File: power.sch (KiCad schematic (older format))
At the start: 43 parts, among them J5 Conn_01x02, Q1 Q_NMOS_GSD, Q2 AON7405, Q3 Q_NMOS_GSD, U7 MP8759GD, U8 NCP133AMX150TCG

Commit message: re-layout power input switcher
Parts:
- R21: footprint Resistor_SMD:R_0402_1005Metric -> Resistor_SMD:R_0603_1608Metric
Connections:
- net FB: now reaches R26.1, R27.2, R29.2, U7.11 (FB)
- net EN: now reaches C93.1, R18.2, R19.1, U7.12 (EN)
- net MODE: now reaches R20.1, R22.1, U7.6 (MODE)
- net SW: now reaches C94.2, L7.1, R25.2, U7.7 (SW)
- net BST: now reaches R21.2, U7.8 (BST)
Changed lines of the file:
@@
 F 0 "R21" V 6993 1750 50  0000 C CNN
 F 1 "3.3" V 7084 1750 50  0000 C CNN
-F 2 "Resistor_SMD:R_0402_1005Metric" V 7130 1750 50  0001 C CNN
+F 2 "Resistor_SMD:R_0603_1608Metric" V 7130 1750 50  0001 C CNN
 F 3 "~" H 7200 1750 50  0001 C CNN
 	1    7200 1750
@@
 Wire Wire Line
 	2600 3600 2700 3600
+Text Label 7350 2500 0    50   ~ 0
+SW
+Text Label 7350 3150 0    50   ~ 0
+FB
+Text Label 5750 2850 0    50   ~ 0
+EN
+Text Label 6100 3250 0    50   ~ 0
+MODE
+Text Label 6800 2100 0    50   ~ 0
+BST
 $EndSCHEMATC

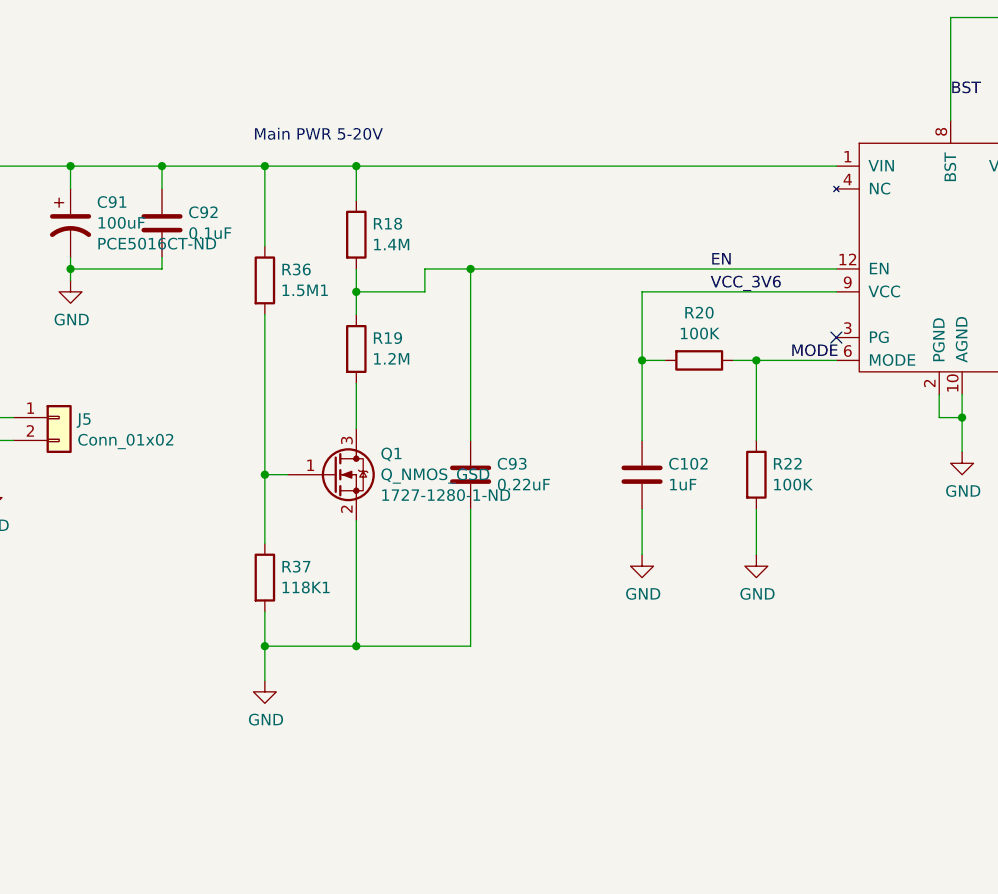
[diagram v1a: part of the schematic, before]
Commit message: Add zener instead of fet to limit voltage on power input EN
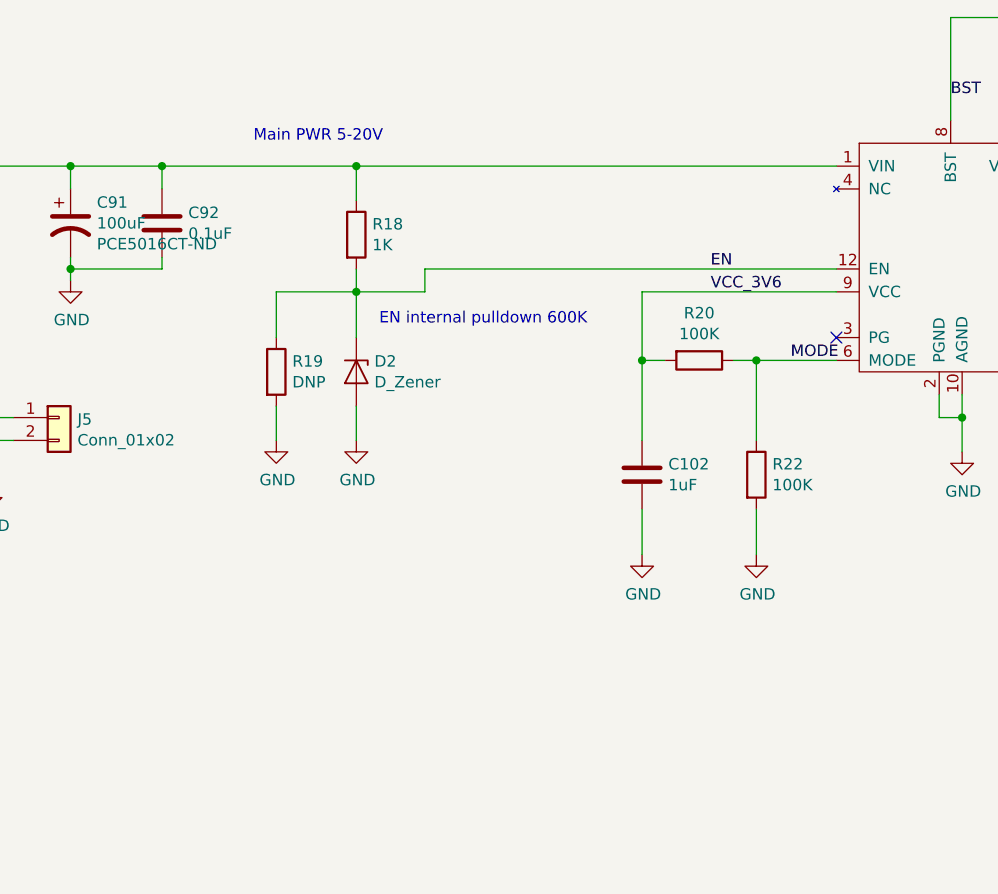
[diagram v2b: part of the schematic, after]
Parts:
- removed C93: 0.22uF, Capacitor_SMD:C_0402_1005Metric, symbol Device:C
- removed Q1: Q_NMOS_GSD, Package_TO_SOT_SMD:SOT-323_SC-70, symbol Device:Q_NMOS_GSD
- removed R36: 1.5M1, Resistor_SMD:R_0402_1005Metric, symbol Device:R
- removed R37: 118K1, Resistor_SMD:R_0402_1005Metric, symbol Device:R
- added D2: D_Zener, Diode_SMD:D_SOD-323, symbol Device:D_Zener
- R18: value 1.4M -> 1K
- R19: value 1.2M -> DNP
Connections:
- net EN: now also D2.1 (K)
- net GND: now also R19.2, D2.2 (A)
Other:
- note added: "EN internal pulldown 600K"
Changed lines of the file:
@@
 EESchema Schematic File Version 4
+LIBS:mxenc-cache
 EELAYER 29 0
 EELAYER END
@@
 	6300 2400 4200 2400
 $Comp
-L Device:Q_NMOS_GSD Q1
-U 1 1 5DC87C75
-P 4100 3750
-F 0 "Q1" H 4306 3841 50  0000 L CNN
-F 1 "Q_NMOS_GSD" H 4306 3750 50  0000 L CNN
-F 2 "Package_TO_SOT_SMD:SOT-323_SC-70" H 4300 3850 50  0001 C CNN
-F 3 "~" H 4100 3750 50  0001 C CNN
-F 4 "1727-1280-1-ND" H 4306 3659 50  0000 L CNN "Vendorpart"
-F 5 "NX3008NBKW,115" H 4100 3750 50  0001 C CNN "Part"
-	1    4100 3750
-	1    0    0    -1
-$EndComp
-$Comp
-L Device:R R36
-U 1 1 5DC8BFE6
-P 3800 2900
-F 0 "R36" H 3870 2946 50  0000 L CNN
-F 1 "1.5M1" H 3870 2855 50  0000 L CNN
-F 2 "Resistor_SMD:R_0402_1005Metric" V 3730 2900 50  0001 C CNN
-F 3 "~" H 3800 2900 50  0001 C CNN
-	1    3800 2900
-	1    0    0    -1
-$EndComp
-$Comp
-L Device:R R37
-U 1 1 5DC8C35A
-P 3800 4200
-F 0 "R37" H 3870 4246 50  0000 L CNN
-F 1 "118K1" H 3870 4155 50  0000 L CNN
-F 2 "Resistor_SMD:R_0402_1005Metric" V 3730 4200 50  0001 C CNN
-F 3 "~" H 3800 4200 50  0001 C CNN
-	1    3800 4200
-	1    0    0    -1
-$EndComp
-$Comp
 L Device:R R18
 U 1 1 5DC8CB6A
 P 4200 2700
 F 0 "R18" H 4270 2746 50  0000 L CNN
-F 1 "1.4M" H 4270 2655 50  0000 L CNN
+F 1 "1K" H 4270 2655 50  0000 L CNN
 F 2 "Resistor_SMD:R_0402_1005Metric" V 4130 2700 50  0001 C CNN
 F 3 "~" H 4200 2700 50  0001 C CNN
 	1    4200 2700
-	1    0    0    -1
-$EndComp
-$Comp
-L Device:R R19
-U 1 1 5DC8D48B
-P 4200 3200
-F 0 "R19" H 4270 3246 50  0000 L CNN
-F 1 "1.2M" H 4270 3155 50  0000 L CNN
-F 2 "Resistor_SMD:R_0402_1005Metric" V 4130 3200 50  0001 C CNN
-F 3 "~" H 4200 3200 50  0001 C CNN
-	1    4200 3200
 	1    0    0    -1
 $EndComp
@@
 	3350 2400 2950 2400
 Wire Wire Line
-	3800 2400 3800 2750
-Connection ~ 3800 2400
-Wire Wire Line
-	3800 2400 3350 2400
-Wire Wire Line
-	3800 3050 3800 3750
-Wire Wire Line
-	3800 3750 3900 3750
-Wire Wire Line
-	3800 3750 3800 4050
-Connection ~ 3800 3750
-Wire Wire Line
-	4200 3550 4200 3350
-Wire Wire Line
-	4200 3050 4200 2950
-Wire Wire Line
 	4200 2550 4200 2400
 Connection ~ 4200 2400
 Wire Wire Line
-	4200 2400 3800 2400
-Wire Wire Line
 	4200 2950 4500 2950
 Wire Wire Line
@@
 Wire Wire Line
 	4200 2950 4200 2850
-Wire Wire Line
-	4200 3950 4200 4500
-Wire Wire Line
-	4200 4500 3800 4500
-Wire Wire Line
-	3800 4500 3800 4350
-$Comp
-L power:GND #PWR0165
-U 1 1 5DC9B92E
-P 3800 4650
-F 0 "#PWR0165" H 3800 4400 50  0001 C CNN
-F 1 "GND" H 3805 4477 50  0000 C CNN
-F 2 "" H 3800 4650 50  0001 C CNN
-F 3 "" H 3800 4650 50  0001 C CNN
-	1    3800 4650
-	1    0    0    -1
-$EndComp
-Wire Wire Line
-	3800 4650 3800 4500
-Connection ~ 3800 4500
-$Comp
-L Device:C C93
-U 1 1 5DC9C3FB
-P 4700 3750
-F 0 "C93" H 4815 3796 50  0000 L CNN
-F 1 "0.22uF" H 4815 3705 50  0000 L CNN
-F 2 "Capacitor_SMD:C_0402_1005Metric" H 4738 3600 50  0001 C CNN
-F 3 "~" H 4700 3750 50  0001 C CNN
-	1    4700 3750
-	1    0    0    -1
-$EndComp
-Wire Wire Line
-	4700 3900 4700 4500
-Wire Wire Line
-	4700 4500 4200 4500
-Connection ~ 4200 4500
-Wire Wire Line
-	4700 3600 4700 2850
-Wire Wire Line
-	4500 2850 4700 2850
-Connection ~ 4700 2850
 Wire Wire Line
 	5950 3250 5950 3600
@@
 Wire Wire Line
 	5450 4100 5450 3900
-Wire Wire Line
-	4700 2850 6300 2850
 Wire Wire Line
 	5450 3250 5450 2950
@@
 Text Label 6800 2100 0    50   ~ 0
 BST
+Wire Wire Line
+	4500 2850 6300 2850
+Wire Wire Line
+	3350 2400 4200 2400
+$Comp
+L power:GND #PWR0165
+U 1 1 5DC6150E
+P 4200 3600
+F 0 "#PWR0165" H 4200 3350 50  0001 C CNN
+F 1 "GND" H 4205 3427 50  0000 C CNN
+F 2 "" H 4200 3600 50  0001 C CNN
+F 3 "" H 4200 3600 50  0001 C CNN
+	1    4200 3600
+	1    0    0    -1
+$EndComp
+$Comp
+L Device:D_Zener D2
+U 1 1 5DC62380
+P 4200 3300
+F 0 "D2" V 4154 3379 50  0000 L CNN
+F 1 "D_Zener" V 4245 3379 50  0000 L CNN
+F 2 "Diode_SMD:D_SOD-323" H 4200 3300 50  0001 C CNN
+F 3 "~" H 4200 3300 50  0001 C CNN
+F 4 "MM3Z4V3ST1GOSCT-ND" H 4200 3300 50  0001 C CNN "Vendorpart"
+F 5 "MM3Z4V3ST1G" H 4200 3300 50  0001 C CNN "Part"
+	1    4200 3300
+	0    1    1    0
+$EndComp
+Wire Wire Line
+	4200 2950 4200 3150
+Wire Wire Line
+	4200 3600 4200 3450
+Text Notes 4300 3100 0    50   ~ 0
+EN internal pulldown 600K
+$Comp
+L Device:R R19
+U 1 1 5D9BE1EB
+P 3850 3300
+F 0 "R19" H 3920 3346 50  0000 L CNN
+F 1 "DNP" H 3920 3255 50  0000 L CNN
+F 2 "Resistor_SMD:R_0402_1005Metric" V 3780 3300 50  0001 C CNN
+F 3 "~" H 3850 3300 50  0001 C CNN
+	1    3850 3300
+	1    0    0    -1
+$EndComp
+$Comp
+L power:GND #PWR0262
+U 1 1 5D9BE857
+P 3850 3600
+F 0 "#PWR0262" H 3850 3350 50  0001 C CNN
+F 1 "GND" H 3855 3427 50  0000 C CNN
+F 2 "" H 3850 3600 50  0001 C CNN
+F 3 "" H 3850 3600 50  0001 C CNN
+	1    3850 3600
+	1    0    0    -1
+$EndComp
+Wire Wire Line
+	3850 3600 3850 3450
+Wire Wire Line
+	3850 3150 3850 2950
+Wire Wire Line
+	3850 2950 4200 2950
 $EndSCHEMATC

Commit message: improved 5v power supply routing
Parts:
- R23: footprint Resistor_SMD:R_0402_1005Metric -> Resistor_SMD:R_0805_2012Metric
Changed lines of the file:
@@
 F 0 "R23" V 10693 2400 50  0000 C CNN
 F 1 "0" V 10784 2400 50  0000 C CNN
-F 2 "Resistor_SMD:R_0402_1005Metric" V 10830 2400 50  0001 C CNN
+F 2 "Resistor_SMD:R_0805_2012Metric" V 10830 2400 50  0001 C CNN
 F 3 "~" H 10900 2400 50  0001 C CNN
 	1    10900 2400

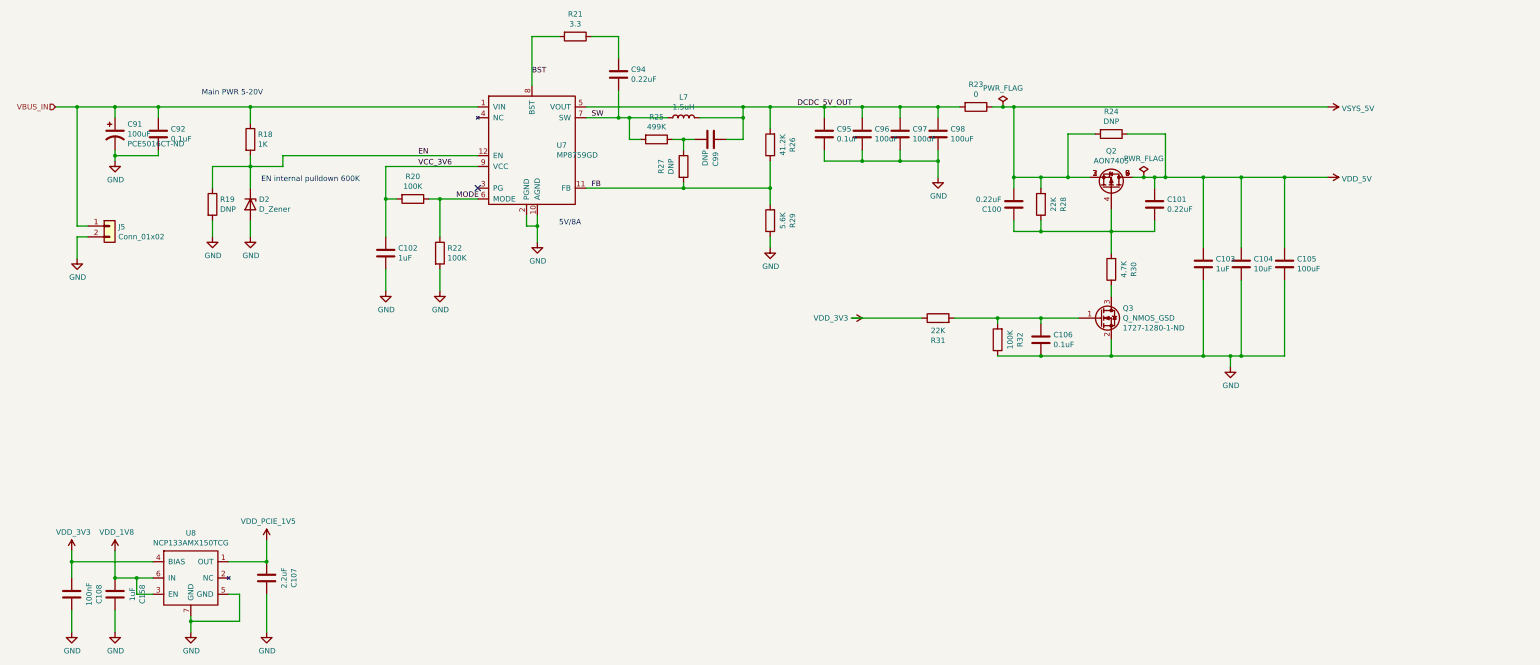
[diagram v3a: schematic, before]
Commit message: Complete entry of bom
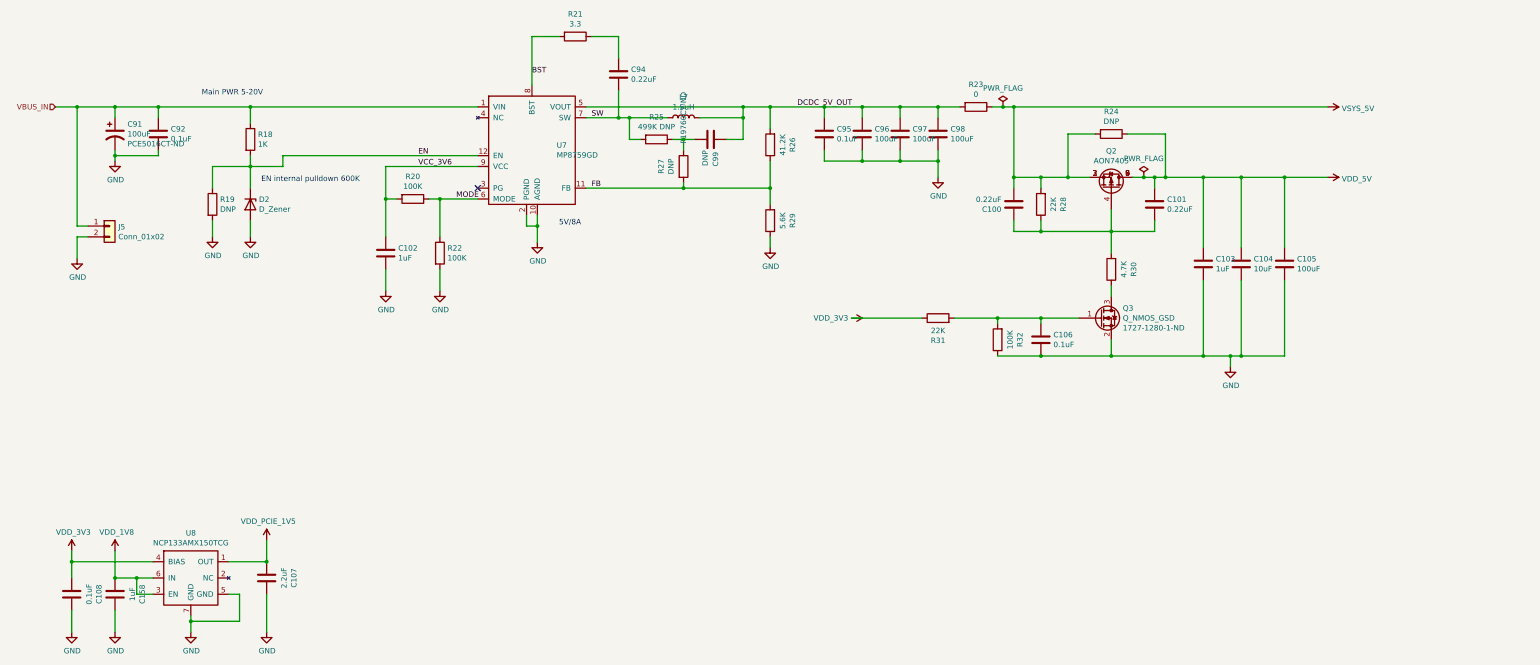
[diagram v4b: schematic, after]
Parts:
- C100, C101, C94: Mfgr (none) -> Murata; Part (none) -> GRM155C8YA224ME01D; Vendorpart (none) -> 490-10446-1-ND
- C102, C103: Mfgr (none) -> Murata; Part (none) -> GRM155C81A105KA12D; Vendorpart (none) -> 490-12699-1-ND
- C104: Mfgr (none) -> Samsung; Part (none) -> CL21X106KPYNNNE; Vendorpart (none) -> 1276-3025-1-ND
- C105, C96, C97, C98: Mfgr (none) -> Murata; Part (none) -> GRM32EC70J107ME15L; Vendorpart (none) -> 490-10530-1-ND
- C106, C92, C95: Mfgr (none) -> Murata; Part (none) -> GRM155R71E104KE14J; Vendorpart (none) -> 490-14603-1-ND
- C107: footprint Resistor_SMD:R_0402_1005Metric -> Capacitor_SMD:C_0402_1005Metric; Mfgr (none) -> Murata; Part (none) -> GRM155C80J225ME95D; Vendorpart (none) -> 490-10013-1-ND
- C108: value 100nF -> 0.1uF; footprint Resistor_SMD:R_0201_0603Metric -> Capacitor_SMD:C_0201_0603Metric; Mfgr (none) -> Murata; Part (none) -> GRM033C80J104KE15D; Vendorpart (none) -> 490-10390-1-ND
- C158: footprint Resistor_SMD:R_0402_1005Metric -> Capacitor_SMD:C_0402_1005Metric; Mfgr (none) -> Murata; Part (none) -> GRM155C81A105KA12D; Vendorpart (none) -> 490-12699-1-ND
- C91: Mfgr (none) -> Panasonic
- D2: Mfgr (none) -> ON
- J5: Mfgr (none) -> JST; Part (none) -> SM02B-GHS-TB(LF)(SN); Vendorpart (none) -> 455-1564-1-ND
- L7: Mfgr (none) -> Panasonic; Part (none) -> ETQ-P3M1R5KVP; Vendorpart (none) -> P19760CT-ND
- Q2: Mfgr (none) -> AOS; Part (none) -> AON7405; Vendorpart (none) -> 785-1305-1-ND
- R18: Mfgr (none) -> Yageo; Part (none) -> RC0402JR-071KL; Vendorpart (none) -> 311-1.0KJRCT-ND
- R20, R22, R32: Mfgr (none) -> Yageo; Part (none) -> RC0402JR-07100KL; Vendorpart (none) -> 311-100KJRCT-ND
- R21: Mfgr (none) -> Vishay Beyschlag; Part (none) -> MCT06030C3308FP500; Vendorpart (none) -> 749-1639-1-ND
- R23: Mfgr (none) -> Vishay Dale; Part (none) -> CRCW08050000Z0EAHP; Vendorpart (none) -> 541-0.0TBCT-ND
- R25: value 499K -> 499K DNP
- R26: Mfgr (none) -> Panasonic; Part (none) -> ERJ-2RKF4122X; Vendorpart (none) -> P41.2KLCT-ND
- R28, R31: Mfgr (none) -> Panasonic; Part (none) -> ERJ-2GEJ223X; Vendorpart (none) -> P22KJCT-ND
- R29: Mfgr (none) -> Panasonic; Part (none) -> ERJ-2RKF5601X; Vendorpart (none) -> P5.60KLCT-ND
- R30: Mfgr (none) -> Panasonic; Part (none) -> ERJ-2RKF4701X; Vendorpart (none) -> P4.70KLCT-ND
- U7: Mfgr (none) -> MP; Part (none) -> MP8759GD-Z; Vendorpart (none) -> 1589-1736-1-ND
- U8: Mfgr (none) -> ON; Part (none) -> NCP133AMX150TCG

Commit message: wip more new layout
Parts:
- L7: footprint Inductor_SMD:L_6.3x6.3_H3 -> Inductor_SMD:L_Wuerth_MAPI-4020; Mfgr Panasonic -> Würth; Part ETQ-P3M1R5KVP -> 74438357015; Vendorpart P19760CT-ND -> 732-11199-1-ND
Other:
- note added: "AON2405 is EOL. Possible replacement\nhttps://www.digikey.com/product-detail/en/0/785-AONR21305CTR-ND"
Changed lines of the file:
@@
 $Descr USLedger 17000 11000
 encoding utf-8
-Sheet 7 9
+Sheet 7 10
 Title ""
 Date ""
@@
 F 0 "L7" V 8390 2500 50  0000 C CNN
 F 1 "1.5uH" V 8299 2500 50  0000 C CNN
-F 2 "Inductor_SMD:L_6.3x6.3_H3" H 8200 2500 50  0001 C CNN
+F 2 "Inductor_SMD:L_Wuerth_MAPI-4020" H 8200 2500 50  0001 C CNN
 F 3 "~" H 8200 2500 50  0001 C CNN
-F 4 "P19760CT-ND" H 8200 2500 50  0000 C CNN "Vendorpart"
-F 5 "Panasonic" H 8200 2500 50  0001 C CNN "Mfgr"
-F 6 "ETQ-P3M1R5KVP" H 8200 2500 50  0001 C CNN "Part"
+F 4 "732-11199-1-ND" H 8200 2500 50  0000 C CNN "Vendorpart"
+F 5 "Würth" H 8200 2500 50  0001 C CNN "Mfgr"
+F 6 "74438357015" H 8200 2500 50  0001 C CNN "Part"
 	1    8200 2500
 	0    -1   -1   0
@@
 Wire Wire Line
 	3850 2950 4200 2950
+Text Notes 12800 2750 0    50   ~ 0
+AON2405 is EOL. Possible replacement\nhttps://www.digikey.com/product-detail/en/0/785-AONR21305CTR-ND
 $EndSCHEMATC

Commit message: rerouted sd, added some gpio, started power input
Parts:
- J5: footprint Connector_JST:JST_GH_SM02B-GHS-TB_1x02-1MP_P1.25mm_Horizontal -> Connector_JST:JST_XH_B2B-XH-A_1x02_P2.50mm_Vertical
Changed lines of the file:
@@
 F 0 "J5" H 2980 3492 50  0000 L CNN
 F 1 "Conn_01x02" H 2980 3401 50  0000 L CNN
-F 2 "Connector_JST:JST_GH_SM02B-GHS-TB_1x02-1MP_P1.25mm_Horizontal" H 2900 3500 50  0001 C CNN
+F 2 "Connector_JST:JST_XH_B2B-XH-A_1x02_P2.50mm_Vertical" H 2900 3500 50  0001 C CNN
 F 3 "~" H 2900 3500 50  0001 C CNN
 F 4 "JST" H 2900 3500 50  0001 C CNN "Mfgr"

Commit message: Finish remaining routing
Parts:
- removed C91: 100uF, Capacitor_SMD:C_Elec_6.3x5.8, symbol Device:CP1
- removed R23: 0, Resistor_SMD:R_0805_2012Metric, symbol Device:R
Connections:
- net DCDC_5V_OUT is gone; now on net VSYS_5V: C95.1, C96.1, C97.1, C98.1, C99.1, L7.2, R26.2, U7.5 (VOUT)
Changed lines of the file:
@@
-$EndComp
-$Comp
-L Device:CP1 C91
-U 1 1 5DC98E6E
-P 2950 2650
-F 0 "C91" H 3065 2741 50  0000 L CNN
-F 1 "100uF" H 3065 2650 50  0000 L CNN
-F 2 "Capacitor_SMD:C_Elec_6.3x5.8" H 2950 2650 50  0001 C CNN
-F 3 "~" H 2950 2650 50  0001 C CNN
-F 4 "PCE5016CT-ND" H 3065 2559 50  0000 L CNN "Vendorpart"
-F 5 "EEE-FT1V101AP" H 2950 2650 50  0001 C CNN "Part"
-F 6 "Panasonic" H 2950 2650 50  0001 C CNN "Mfgr"
-	1    2950 2650
-	1    0    0    -1
 $EndComp
 $Comp
@@
 L power:GND #PWR0164
 U 1 1 5DC99486
-P 2950 2900
-F 0 "#PWR0164" H 2950 2650 50  0001 C CNN
-F 1 "GND" H 2955 2727 50  0000 C CNN
-F 2 "" H 2950 2900 50  0001 C CNN
-F 3 "" H 2950 2900 50  0001 C CNN
-	1    2950 2900
-	1    0    0    -1
-$EndComp
-Wire Wire Line
-	2950 2900 2950 2850
-Wire Wire Line
-	3350 2800 3350 2850
-Wire Wire Line
-	3350 2850 2950 2850
-Connection ~ 2950 2850
-Wire Wire Line
-	2950 2850 2950 2800
-Wire Wire Line
-	2950 2500 2950 2400
-Connection ~ 2950 2400
+P 3350 2900
+F 0 "#PWR0164" H 3350 2650 50  0001 C CNN
+F 1 "GND" H 3355 2727 50  0000 C CNN
+F 2 "" H 3350 2900 50  0001 C CNN
+F 3 "" H 3350 2900 50  0001 C CNN
+	1    3350 2900
+	1    0    0    -1
+$EndComp
 Wire Wire Line
 	3350 2500 3350 2400
 Connection ~ 3350 2400
-Wire Wire Line
-	3350 2400 2950 2400
 Wire Wire Line
 	4200 2550 4200 2400
@@
 Text Label 5750 2950 0    50   ~ 0
 VCC_3V6
-Wire Wire Line
-	2600 2400 2950 2400
 $Comp
 L Connector_Generic:Conn_01x02 J?
@@
 Wire Wire Line
 	10200 2900 9850 2900
-$Comp
-L Device:R R23
-U 1 1 5DD1DBCF
-P 10900 2400
-F 0 "R23" V 10693 2400 50  0000 C CNN
-F 1 "0" V 10784 2400 50  0000 C CNN
-F 2 "Resistor_SMD:R_0805_2012Metric" V 10830 2400 50  0001 C CNN
-F 3 "~" H 10900 2400 50  0001 C CNN
-F 4 "Vishay Dale" H 10900 2400 50  0001 C CNN "Mfgr"
-F 5 "CRCW08050000Z0EAHP" H 10900 2400 50  0001 C CNN "Part"
-F 6 "541-0.0TBCT-ND" H 10900 2400 50  0001 C CNN "Vendorpart"
-	1    10900 2400
-	0    1    1    0
-$EndComp
-Wire Wire Line
-	10550 2400 10750 2400
 Connection ~ 10550 2400
 Wire Wire Line
@@
 Wire Wire Line
 	12650 3050 12550 3050
-Text Label 9250 2400 0    50   ~ 0
-DCDC_5V_OUT
 $Comp
 L mxenc:VSYS_5V #PWR0179
@@
 Connection ~ 11150 2400
 Wire Wire Line
-	11150 2400 11050 2400
-Wire Wire Line
 	2600 3500 2700 3500
 Wire Wire Line
@@
 Text Notes 12800 2750 0    50   ~ 0
 AON2405 is EOL. Possible replacement\nhttps://www.digikey.com/product-detail/en/0/785-AONR21305CTR-ND
+Wire Wire Line
+	2600 2400 3350 2400
+Wire Wire Line
+	3350 2800 3350 2900
+Wire Wire Line
+	10550 2400 11150 2400
 $EndSCHEMATC
